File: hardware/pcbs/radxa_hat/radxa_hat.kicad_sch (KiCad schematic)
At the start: 10 parts, among them J1 RADXA_HEADER, J2 Header_01x06, J3 Header_01x04, J4 Header_01x08, J5 Header_01x04

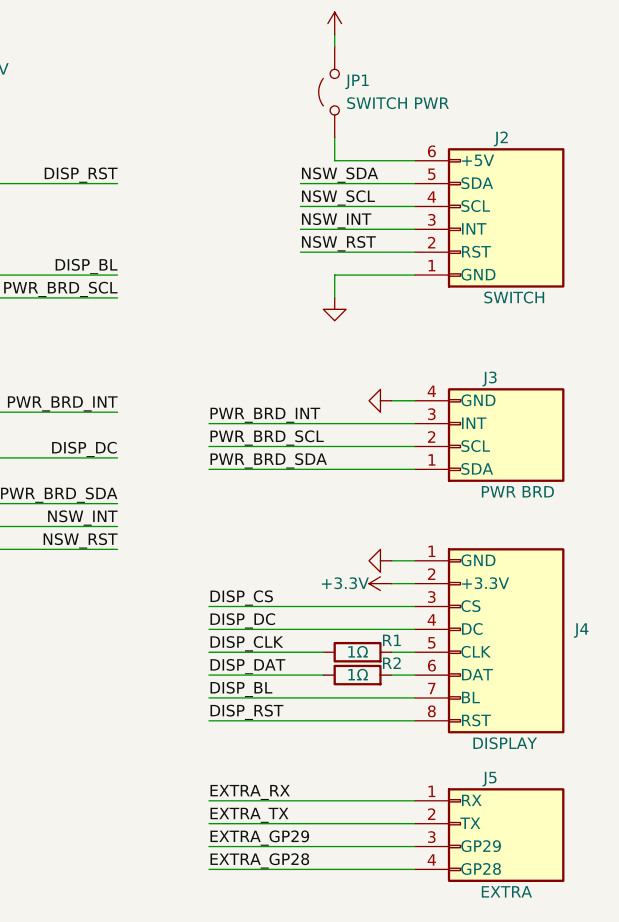
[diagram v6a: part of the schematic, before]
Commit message: boards: fix many silly bugs discovered during testing
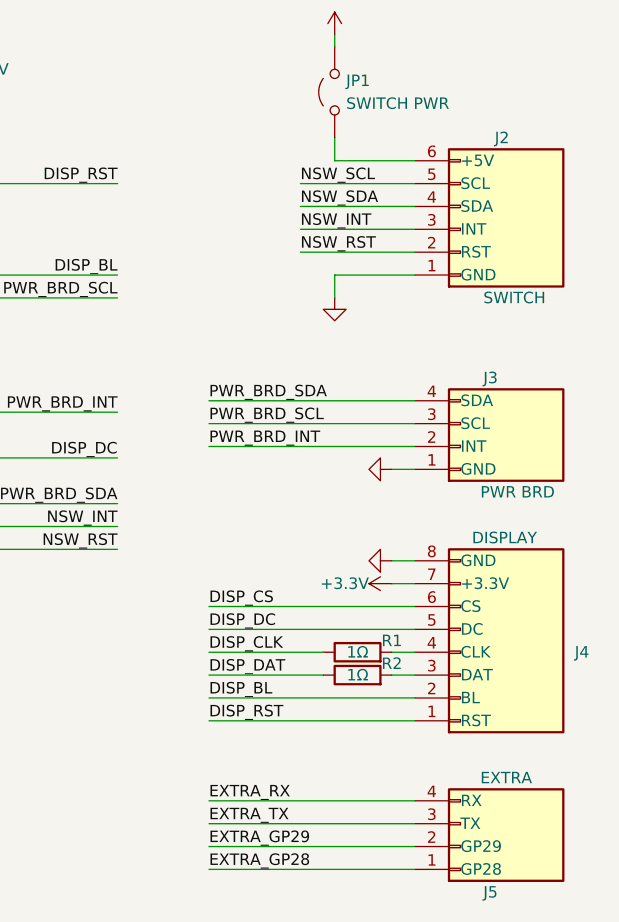
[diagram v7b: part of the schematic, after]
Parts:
- J2: Purpose Pin4 SCL -> SDA; Purpose Pin5 SDA -> SCL
- J3: Purpose Pin1 SDA -> GND; Purpose Pin2 SCL -> INT; Purpose Pin3 INT -> SCL; Purpose Pin4 GND -> SDA
- J4: Purpose Pin1 GND -> RST; Purpose Pin2 +3.3V -> BL; Purpose Pin3 CS -> DAT; Purpose Pin4 DC -> CLK; Purpose Pin5 CLK -> DC; Purpose Pin6 DAT -> CS; Purpose Pin7 BL -> +3.3V; Purpose Pin8 RST -> GND
- J5: Purpose Pin1 RX -> GP28; Purpose Pin2 TX -> GP29; Purpose Pin3 GP29 -> TX; Purpose Pin4 GP28 -> RX
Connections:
- net +3.3V: now also J4.7 (Pin_7); no longer J4.2 (Pin_2)
- net DISP_BL: now also J4.2 (Pin_2); no longer J4.7 (Pin_7)
- net DISP_CS: now also J4.6 (Pin_6); no longer J4.3 (Pin_3)
- net DISP_DC: now also J4.5 (Pin_5); no longer J4.4 (Pin_4)
- net DISP_RST: now also J4.1 (Pin_1); no longer J4.8 (Pin_8)
- net EXTRA_GP28: now also J5.1 (Pin_1); no longer J5.4 (Pin_4)
- net EXTRA_GP29: now also J5.2 (Pin_2); no longer J5.3 (Pin_3)
- net EXTRA_RX: now also J5.4 (Pin_4); no longer J5.1 (Pin_1)
- net EXTRA_TX: now also J5.3 (Pin_3); no longer J5.2 (Pin_2)
- net GND: now also J3.1 (Pin_1), J4.8 (Pin_8); no longer J3.4 (Pin_4), J4.1 (Pin_1)
- net NSW_SCL: now also J2.5 (Pin_5); no longer J2.4 (Pin_4)
- net NSW_SDA: now also J2.4 (Pin_4); no longer J2.5 (Pin_5)
- net PWR_BRD_INT: now also J3.2 (Pin_2); no longer J3.3 (Pin_3)
- net PWR_BRD_SCL: now also J3.3 (Pin_3); no longer J3.2 (Pin_2)
- net PWR_BRD_SDA: now also J3.4 (Pin_4); no longer J3.1 (Pin_1)
- net at R1.2: now also J4.4 (Pin_4); no longer J4.5 (Pin_5)
- net at R2.2: now also J4.3 (Pin_3); no longer J4.6 (Pin_6)
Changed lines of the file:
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@@
 	(wire
 		(pts
-			(xy 182.88 91.44) (xy 205.74 91.44)
+			(xy 182.88 88.9) (xy 205.74 88.9)
 		)
 		(stroke
@@
 	(wire
 		(pts
-			(xy 182.88 88.9) (xy 205.74 88.9)
+			(xy 182.88 91.44) (xy 205.74 91.44)
 		)
 		(stroke
@@
 	(wire
 		(pts
-			(xy 182.88 93.98) (xy 205.74 93.98)
+			(xy 182.88 86.36) (xy 205.74 86.36)
 		)
 		(stroke
@@
 	(wire
 		(pts
-			(xy 203.2 86.36) (xy 205.74 86.36)
+			(xy 203.2 93.98) (xy 205.74 93.98)
 		)
 		(stroke
@@
 	)
 	(label "NSW_SCL"
-		(at 193.04 64.77 0)
+		(at 193.04 62.23 0)
 		(fields_autoplaced yes)
 		(effects
@@
 	)
 	(label "NSW_SDA"
-		(at 193.04 62.23 0)
+		(at 193.04 64.77 0)
 		(fields_autoplaced yes)
 		(effects
@@
 	)
 	(label "PWR_BRD_SDA"
-		(at 182.88 93.98 0)
+		(at 182.88 86.36 0)
 		(fields_autoplaced yes)
 		(effects
@@
 	)
 	(label "PWR_BRD_SCL"
-		(at 182.88 91.44 0)
+		(at 182.88 88.9 0)
 		(fields_autoplaced yes)
 		(effects
@@
 	)
 	(label "PWR_BRD_INT"
-		(at 182.88 88.9 0)
+		(at 182.88 91.44 0)
 		(fields_autoplaced yes)
 		(effects
@@
 	(symbol
 		(lib_id "power:GND")
-		(at 203.2 86.36 270)
+		(at 203.2 93.98 270)
+		(mirror x)
 		(unit 1)
 		(exclude_from_sim no)
@@
 		(fields_autoplaced yes)
 		(property "Reference" "#PWR015"
-			(at 196.85 86.36 0)
+			(at 196.85 93.98 0)
 			(effects
 				(font
@@
 		)
 		(property "Value" "GND"
-			(at 198.12 86.36 0)
+			(at 198.12 93.98 0)
 			(effects
 				(font
@@
 		)
 		(property "Footprint" ""
-			(at 203.2 86.36 0)
+			(at 203.2 93.98 0)
 			(effects
 				(font
@@
 		)
 		(property "Datasheet" ""
-			(at 203.2 86.36 0)
+			(at 203.2 93.98 0)
 			(effects
 				(font
@@
 		)
 		(property "Description" "Power symbol creates a global label with name \"GND\" , ground"
-			(at 203.2 86.36 0)
+			(at 203.2 93.98 0)
 			(effects
 				(font
@@
 			)
 		)
-		(property "Purpose Pin1" "SDA"
+		(property "Purpose Pin1" "GND"
 			(at 210.82 93.98 0)
 			(effects
@@
 			)
 		)
-		(property "Purpose Pin2" "SCL"
+		(property "Purpose Pin2" "INT"
 			(at 210.82 91.44 0)
 			(effects
@@
 			)
 		)
-		(property "Purpose Pin3" "INT"
+		(property "Purpose Pin3" "SCL"
 			(at 210.82 88.9 0)
 			(effects
@@
 			)
 		)
-		(property "Purpose Pin4" "GND"
+		(property "Purpose Pin4" "SDA"
 			(at 210.82 86.36 0)
 			(effects
@@
 			)
 		)
-		(property "Purpose Pin4" "SCL"
+		(property "Purpose Pin4" "SDA"
 			(at 210.82 64.77 0)
 			(do_not_autoplace yes)
@@
 			)
 		)
-		(property "Purpose Pin5" "SDA"
+		(property "Purpose Pin5" "SCL"
 			(at 210.82 62.23 0)
 			(do_not_autoplace yes)
@@
 	(symbol
 		(lib_id "conn:Conn_01x08")
-		(at 210.82 106.68 0)
+		(at 210.82 119.38 0)
+		(mirror x)
 		(unit 1)
 		(exclude_from_sim no)
@@
 		(dnp no)
 		(property "Reference" "J4"
-			(at 223.52 111.7599 0)
+			(at 223.52 114.3001 0)
 			(effects
 				(font
@@
 		)
 		(property "Value" "Header_01x08"
-			(at 215.646 124.46 0)
+			(at 215.646 101.6 0)
 			(effects
 				(font
@@
 		)
 		(property "Footprint" "Connector_MTA-100:mta100_01x8_P2.54_640455-8"
-			(at 210.82 102.362 0)
+			(at 210.82 123.698 0)
 			(effects
 				(font
@@
 		)
 		(property "Datasheet" "~"
-			(at 210.82 106.68 0)
+			(at 210.82 119.38 0)
 			(effects
 				(font
@@
 		)
 		(property "Description" "Generic connector, single row, 01x06, script generated (kicad-library-utils/schlib/autogen/connector/)"
-			(at 211.074 102.362 0)
+			(at 211.074 123.698 0)
 			(effects
 				(font
@@
 			)
 		)
-		(property "Purpose Pin1" "GND"
-			(at 210.82 104.14 0)
+		(property "Purpose Pin1" "RST"
+			(at 210.82 121.92 0)
 			(do_not_autoplace yes)
 			(effects
@@
 			)
 		)
-		(property "Purpose Pin2" "+3.3V"
-			(at 210.82 106.68 0)
+		(property "Purpose Pin2" "BL"
+			(at 210.82 119.38 0)
 			(do_not_autoplace yes)
 			(effects
@@
 			)
 		)
-		(property "Purpose Pin3" "CS"
-			(at 210.82 109.22 0)
+		(property "Purpose Pin3" "DAT"
+			(at 210.82 116.84 0)
 			(do_not_autoplace yes)
 			(effects
@@
 			)
 		)
-		(property "Purpose Pin4" "DC"
-			(at 210.82 111.76 0)
+		(property "Purpose Pin4" "CLK"
+			(at 210.82 114.3 0)
 			(do_not_autoplace yes)
 			(effects
@@
 			)
 		)
-		(property "Purpose Pin5" "CLK"
-			(at 210.82 114.3 0)
+		(property "Purpose Pin5" "DC"
+			(at 210.82 111.76 0)
 			(do_not_autoplace yes)
 			(effects
@@
 			)
 		)
-		(property "Purpose Pin6" "DAT"
-			(at 210.82 116.84 0)
+		(property "Purpose Pin6" "CS"
+			(at 210.82 109.22 0)
 			(do_not_autoplace yes)
 			(effects
@@
 			)
 		)
-		(property "Purpose Pin7" "BL"
-			(at 210.82 119.38 0)
+		(property "Purpose Pin7" "+3.3V"
+			(at 210.82 106.68 0)
 			(do_not_autoplace yes)
 			(effects
@@
 			)
 		)
-		(property "Purpose Pin8" "RST"
-			(at 210.82 121.92 0)
+		(property "Purpose Pin8" "GND"
+			(at 210.82 104.14 0)
 			(do_not_autoplace yes)
 			(effects
@@
 		)
 		(property "Purpose" "DISPLAY"
-			(at 212.09 124.46 0)
+			(at 212.09 101.6 0)
 			(effects
 				(font
@@
 		)
 		(property "Part" "640456-8"
-			(at 210.82 106.68 0)
+			(at 210.82 119.38 0)
 			(effects
 				(font
@@
 		)
 		(property "Shop" "https://eu.mouser.com/ProductDetail/TE-Connectivity-AMP/640456-8?qs=%2F35zJ5USjomho1287DA4QA%3D%3D"
-			(at 210.82 106.68 0)
+			(at 210.82 119.38 0)
 			(effects
 				(font
@@
 	(symbol
 		(lib_id "conn:Conn_01x04")
-		(at 210.82 133.35 0)
+		(at 210.82 135.89 0)
+		(mirror x)
 		(unit 1)
 		(exclude_from_sim no)
@@
 		(dnp no)
 		(property "Reference" "J5"
-			(at 213.36 128.27 0)
+			(at 213.36 140.97 0)
 			(effects
 				(font
@@
 		)
 		(property "Value" "Header_01x04"
-			(at 215.9 140.97 0)
+			(at 215.9 128.27 0)
 			(effects
 				(font
@@
 		)
 		(property "Footprint" "Connector_MTA-100:mta100_01x4_P2.54_640455-4"
-			(at 210.82 133.35 0)
+			(at 210.82 135.89 0)
 			(effects
 				(font
@@
 		)
 		(property "Datasheet" "~"
-			(at 210.82 133.35 0)
+			(at 210.82 135.89 0)
 			(effects
 				(font
@@
 		)
 		(property "Description" ""
-			(at 210.82 133.35 0)
+			(at 210.82 135.89 0)
 			(effects
 				(font
@@
 		)
 		(property "Purpose" "EXTRA"
-			(at 215.9 140.97 0)
+			(at 215.9 128.27 0)
 			(effects
 				(font
@@
 			)
 		)
-		(property "Purpose Pin1" "RX"
-			(at 210.82 130.81 0)
+		(property "Purpose Pin1" "GP28"
+			(at 210.82 138.43 0)
 			(effects
 				(font
@@
 			)
 		)
-		(property "Purpose Pin2" "TX"
-			(at 210.82 133.35 0)
+		(property "Purpose Pin2" "GP29"
+			(at 210.82 135.89 0)
 			(effects
 				(font
@@
 			)
 		)
-		(property "Purpose Pin3" "GP29"
-			(at 210.82 135.89 0)
+		(property "Purpose Pin3" "TX"
+			(at 210.82 133.35 0)
 			(effects
 				(font
@@
 			)
 		)
-		(property "Purpose Pin4" "GP28"
-			(at 210.82 138.43 0)
+		(property "Purpose Pin4" "RX"
+			(at 210.82 130.81 0)
 			(effects
 				(font
@@
 		)
 		(property "Shop" "https://eu.mouser.com/ProductDetail/TE-Connectivity-AMP/640456-4?qs=%2F35zJ5USjokX5rl%252BbVBc4g%3D%3D"
-			(at 210.82 133.35 0)
+			(at 210.82 135.89 0)
 			(effects
 				(font
@@
 		)
 		(property "Part" "640456-4"
-			(at 210.82 133.35 0)
+			(at 210.82 135.89 0)
 			(effects
 				(font

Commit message: boards: update mta100 part numbers
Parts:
- J2: Part 640456-6 -> 640457-6; Shop https://eu.mouser.com/ProductDetail/TE-Connectivity-AMP/640456-6?qs=%2F35zJ5USjomb%252BGgX%252BBnrrQ%3D%3D -> https://eu.mouser.com/ProductDetail/TE-Connectivity-AMP/640457-6?qs=%2F35zJ5USjomeIT6dNVSouw%3D%3D
- J3, J5: Part 640456-4 -> 640457-4; Shop https://eu.mouser.com/ProductDetail/TE-Connectivity-AMP/640456-4?qs=%2F35zJ5USjokX5rl%252BbVBc4g%3D%3D -> https://eu.mouser.com/ProductDetail/TE-Connectivity-AMP/640457-4?qs=%2F35zJ5USjomT7VbYP4Jl7Q%3D%3D
- J4: Part 640456-8 -> 640457-8; Shop https://eu.mouser.com/ProductDetail/TE-Connectivity-AMP/640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 -> https://eu.mouser.com/ProductDetail/TE-Connectivity/640457-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
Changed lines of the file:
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@@
 			)
 		)
-		(property "Shop" "https://eu.mouser.com/ProductDetail/TE-Connectivity-AMP/640456-4?qs=%2F35zJ5USjokX5rl%252BbVBc4g%3D%3D"
+		(property "Shop" "https://eu.mouser.com/ProductDetail/TE-Connectivity-AMP/640457-4?qs=%2F35zJ5USjomT7VbYP4Jl7Q%3D%3D"
 			(at 210.82 91.44 0)
 			(effects
@@
 			)
 		)
-		(property "Part" "640456-4"
+		(property "Part" "640457-4"
 			(at 210.82 91.44 0)
 			(effects
@@
 			)
 		)
-		(property "Part" "640456-6"
+		(property "Part" "640457-6"
 			(at 210.82 69.85 0)
 			(effects
@@
 			)
 		)
-		(property "Shop" "https://eu.mouser.com/ProductDetail/TE-Connectivity-AMP/640456-6?qs=%2F35zJ5USjomb%252BGgX%252BBnrrQ%3D%3D"
+		(property "Shop" "https://eu.mouser.com/ProductDetail/TE-Connectivity-AMP/640457-6?qs=%2F35zJ5USjomeIT6dNVSouw%3D%3D"
 			(at 210.82 69.85 0)
 			(effects
@@
 			)
 		)
-		(property "Part" "640456-8"
+		(property "Part" "640457-8"
 			(at 210.82 119.38 0)
 			(effects
@@
 			)
 		)
-		(property "Shop" "https://eu.mouser.com/ProductDetail/TE-Connectivity-AMP/640456-8?qs=%2F35zJ5USjomho1287DA4QA%3D%3D"
+		(property "Shop" "https://eu.mouser.com/ProductDetail/TE-Connectivity/640457-8?qs=%2F35zJ5USjokX8LSglMnOhw%3D%3D"
 			(at 210.82 119.38 0)
 			(effects
@@
 			)
 		)
-		(property "Shop" "https://eu.mouser.com/ProductDetail/TE-Connectivity-AMP/640456-4?qs=%2F35zJ5USjokX5rl%252BbVBc4g%3D%3D"
+		(property "Shop" "https://eu.mouser.com/ProductDetail/TE-Connectivity-AMP/640457-4?qs=%2F35zJ5USjomT7VbYP4Jl7Q%3D%3D"
 			(at 210.82 135.89 0)
 			(effects
@@
 			)
 		)
-		(property "Part" "640456-4"
+		(property "Part" "640457-4"
 			(at 210.82 135.89 0)
 			(effects
